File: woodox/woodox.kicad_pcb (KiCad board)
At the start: 2 copper layers, 162.2 x 126.5 mm, 95 parts, among them IC1 W25Q16JVUXIQ_TR, J1 Conn_01x03_Female, J2 USB_C_Receptacle, SW1 BOOT, SW2 RESET, U1 DRV5057A3, U10 OLED_256x64_I2C, U11 DRV5057A3, U12 DRV5057A3, U13 DRV5057A3, U14 DRV5057A3, U15 DRV5057A3, U16 DRV5057A3, U17 DRV5057A3, U18 DRV5057A3, U19 DRV5057A3, U2 DRV5057A3, U20 DRV5057A3, U21 DRV5057A3, U22 DRV5057A3, U23 DRV5057A3, U24 DRV5057A3, U25 RP2040, U26 DRV5057A3, U27 DRV5057A3, U28 DRV5057A3, U29 DRV5057A3, U3 DRV5057A3, U30 DRV5057A3, U31 DRV5057A3, U32 DRV5057A3, U33 NCP1117-3.3_SOT223, U34 74HC4051, U35 74HC4051, U36 74HC4051, U37 74HC4051, U38 DRV5057A3, U39 DRV5057A3, U4 DRV5057A3, U5 DRV5057A3, U6 DRV5057A3, U7 DRV5057A3, U8 DRV5057A3, U9 DRV5057A3, Y1 ECS-120-8-30-JGN-TR

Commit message: double sided pcb
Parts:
- added C11: 0.1uF, Capacitor_SMD:C_0603_1608Metric, F.Cu at (157.4, 56.4)
- added C12: 27pF, Capacitor_SMD:C_0603_1608Metric, F.Cu at (165.9, 74.1)
- added C13: 27pF, Capacitor_SMD:C_0603_1608Metric, F.Cu at (160.3, 71.8)
- added C14: 1uF, Capacitor_SMD:C_0603_1608Metric, F.Cu at (167.5, 59.4)
- added C15: 1uF, Capacitor_SMD:C_0603_1608Metric, F.Cu at (168.6, 62.4)
- added C16: 10uF, Capacitor_SMD:C_0603_1608Metric, F.Cu at (49.4, 33.0)
- added C17: 0.1uF, Capacitor_SMD:C_0603_1608Metric, F.Cu at (167.5, 57.9)
- added C18: 1uF, Capacitor_SMD:C_0603_1608Metric, F.Cu at (167.5, 60.9)
- added C19: 0.1uF, Capacitor_SMD:C_0603_1608Metric, F.Cu at (167.5, 56.4)
- added C20: 10uF, Capacitor_SMD:C_0603_1608Metric, F.Cu at (49.3, 38.4)
- added IC2: W25Q16JVUXIQ_TR, W25Q16JVUXIQ_TR:SON50P300X200X60-9N, F.Cu at (158.9, 57.9)
- added J4: USB_C_Receptacle, Connector_USB:USB_C_Receptacle_Amphenol_12401610E4-2A, F.Cu at (56.2, 35.0)
- added JP1: SolderJumper_2_Open, Jumper:SolderJumper-2_P1.3mm_Open_Pad1.0x1.5mm, B.Cu at (155.0, 92.5)
- added JP2: SolderJumper_2_Open, Jumper:SolderJumper-2_P1.3mm_Open_Pad1.0x1.5mm, B.Cu at (157.5, 92.5)
- added JP3: SolderJumper_2_Open, Jumper:SolderJumper-2_P1.3mm_Open_Pad1.0x1.5mm, F.Cu at (155.0, 92.5)
- added JP4: SolderJumper_2_Open, Jumper:SolderJumper-2_P1.3mm_Open_Pad1.0x1.5mm, F.Cu at (157.5, 92.5)
- added JP5: SolderJumper_2_Open, Jumper:SolderJumper-2_P1.3mm_Open_Pad1.0x1.5mm, F.Cu at (165.3, 92.0)
- added JP6: SolderJumper_2_Open, Jumper:SolderJumper-2_P1.3mm_Open_Pad1.0x1.5mm, B.Cu at (165.3, 92.0)
- added LED33: MX_SK6812MINI-E, lib:LED_MX_SK6812MINI-R, F.Cu at (45.3, 48.6)
- added LED34: MX_SK6812MINI-E, lib:LED_MX_SK6812MINI-R, F.Cu at (45.3, 67.7)
- added LED35: MX_SK6812MINI-E, lib:LED_MX_SK6812MINI-R, F.Cu at (45.3, 86.7)
- added LED36: MX_SK6812MINI-E, lib:LED_MX_SK6812MINI-R, F.Cu at (45.3, 105.8)
- added LED37: MX_SK6812MINI-E, lib:LED_MX_SK6812MINI-R, F.Cu at (57.3, 124.8)
- added LED38: MX_SK6812MINI-E, lib:LED_MX_SK6812MINI-R, F.Cu at (66.9, 48.6)
- added LED39: MX_SK6812MINI-E, lib:LED_MX_SK6812MINI-R, F.Cu at (66.9, 67.7)
- added LED40: MX_SK6812MINI-E, lib:LED_MX_SK6812MINI-R, F.Cu at (66.9, 86.7)
- added LED41: MX_SK6812MINI-E, lib:LED_MX_SK6812MINI-R, F.Cu at (66.9, 105.8)
- added LED42: MX_SK6812MINI-E, lib:LED_MX_SK6812MINI-R, F.Cu at (85.9, 44.2)
- added LED43: MX_SK6812MINI-E, lib:LED_MX_SK6812MINI-R, F.Cu at (85.9, 63.2)
- added LED44: MX_SK6812MINI-E, lib:LED_MX_SK6812MINI-R, F.Cu at (85.9, 82.3)
- added LED45: MX_SK6812MINI-E, lib:LED_MX_SK6812MINI-R, F.Cu at (85.9, 101.3)
- added LED46: MX_SK6812MINI-E, lib:LED_MX_SK6812MINI-R, F.Cu at (85.9, 120.4)
- added LED47: MX_SK6812MINI-E, lib:LED_MX_SK6812MINI-R, F.Cu at (105.0, 41.6)
- added LED48: MX_SK6812MINI-E, lib:LED_MX_SK6812MINI-R, F.Cu at (105.0, 60.7)
- added LED49: MX_SK6812MINI-E, lib:LED_MX_SK6812MINI-R, F.Cu at (105.0, 79.7)
- added LED50: MX_SK6812MINI-E, lib:LED_MX_SK6812MINI-R, F.Cu at (105.0, 98.8)
- added LED51: MX_SK6812MINI-E, lib:LED_MX_SK6812MINI-R, F.Cu at (105.0, 117.8)
- added LED52: MX_SK6812MINI-E, lib:LED_MX_SK6812MINI-R, F.Cu at (124.0, 44.2)
- added LED53: MX_SK6812MINI-E, lib:LED_MX_SK6812MINI-R, F.Cu at (124.0, 63.2)
- added LED54: MX_SK6812MINI-E, lib:LED_MX_SK6812MINI-R, F.Cu at (124.0, 82.3)
- added LED55: MX_SK6812MINI-E, lib:LED_MX_SK6812MINI-R, F.Cu at (124.0, 101.3)
- added LED56: MX_SK6812MINI-E, lib:LED_MX_SK6812MINI-R, F.Cu at (130.2, 123.6)
- added LED57: MX_SK6812MINI-E, lib:LED_MX_SK6812MINI-R, F.Cu at (143.1, 46.1)
- added LED58: MX_SK6812MINI-E, lib:LED_MX_SK6812MINI-R, F.Cu at (143.1, 65.1)
- added LED59: MX_SK6812MINI-E, lib:LED_MX_SK6812MINI-R, F.Cu at (143.1, 84.2)
- added LED60: MX_SK6812MINI-E, lib:LED_MX_SK6812MINI-R, F.Cu at (143.1, 103.2)
- added LED61: MX_SK6812MINI-E, lib:LED_MX_SK6812MINI-R, F.Cu at (165.6, 109.6)
- added LED62: MX_SK6812MINI-E, lib:LED_MX_SK6812MINI-R, F.Cu at (153.5, 130.5)
- added LED63: MX_SK6812MINI-E, lib:LED_MX_SK6812MINI-R, F.Cu at (182.1, 119.1)
- added LED64: MX_SK6812MINI-E, lib:LED_MX_SK6812MINI-R, F.Cu at (170.0, 140.0)
- added R10: 10k, Resistor_SMD:R_0603_1608Metric, F.Cu at (157.3, 62.0)
- added R11: 1k, Resistor_SMD:R_0603_1608Metric, F.Cu at (165.1, 71.8)
- added R12: 27.4, Resistor_SMD:R_0603_1608Metric, F.Cu at (164.9, 57.2)
- added R13: 27.4, Resistor_SMD:R_0603_1608Metric, F.Cu at (163.4, 57.2)
- added R14: 5k1, Resistor_SMD:R_0603_1608Metric, F.Cu at (63.1, 35.3)
- added R15: 5k1, Resistor_SMD:R_0603_1608Metric, F.Cu at (64.7, 35.3)
- added R16: 1k, Resistor_SMD:R_0603_1608Metric, F.Cu at (170.1, 46.1)
- added R9: 1k, Resistor_SMD:R_0603_1608Metric, F.Cu at (170.1, 50.0)
- added SW3: BOOT, Button_Switch_SMD:SW_Push_1P1T_NO_Vertical_Wuerth_434133025816, F.Cu at (166.5, 50.0)
- added SW4: RESET, Button_Switch_SMD:SW_Push_1P1T_NO_Vertical_Wuerth_434133025816, F.Cu at (166.5, 46.1)
- added U40: DRV5057A3, lib:DRV505x, F.Cu at (45.3, 48.6)
- added U41: DRV5057A3, lib:DRV505x, F.Cu at (45.3, 67.6)
- added U42: DRV5057A3, lib:DRV505x, F.Cu at (45.3, 86.7)
- added U43: DRV5057A3, lib:DRV505x, F.Cu at (45.3, 105.7)
- added U44: DRV5057A3, lib:DRV505x, F.Cu at (57.4, 124.8)
- added U45: DRV5057A3, lib:DRV505x, F.Cu at (66.9, 48.6)
- added U46: DRV5057A3, lib:DRV505x, F.Cu at (66.9, 67.6)
- added U47: DRV5057A3, lib:DRV505x, F.Cu at (66.9, 86.7)
- added U48: DRV5057A3, lib:DRV505x, F.Cu at (66.9, 105.7)
- added U50: DRV5057A3, lib:DRV505x, F.Cu at (86.0, 44.2)
- added U51: DRV5057A3, lib:DRV505x, F.Cu at (86.0, 63.2)
- added U52: DRV5057A3, lib:DRV505x, F.Cu at (86.0, 82.3)
- added U53: DRV5057A3, lib:DRV505x, F.Cu at (86.0, 101.3)
- added U54: DRV5057A3, lib:DRV505x, F.Cu at (86.0, 120.3)
- added U55: DRV5057A3, lib:DRV505x, F.Cu at (105.0, 41.6)
- added U56: DRV5057A3, lib:DRV505x, F.Cu at (105.0, 60.7)
- added U57: DRV5057A3, lib:DRV505x, F.Cu at (105.0, 79.7)
- added U58: DRV5057A3, lib:DRV505x, F.Cu at (105.0, 98.8)
- added U59: DRV5057A3, lib:DRV505x, F.Cu at (105.0, 117.8)
- added U60: DRV5057A3, lib:DRV505x, F.Cu at (124.1, 44.2)
- added U61: DRV5057A3, lib:DRV505x, F.Cu at (124.1, 63.2)
- added U62: DRV5057A3, lib:DRV505x, F.Cu at (124.1, 82.3)
- added U63: DRV5057A3, lib:DRV505x, F.Cu at (124.1, 101.3)
- added U64: RP2040, Package_DFN_QFN:QFN-56-1EP_7x7mm_P0.4mm_EP3.2x3.2mm, F.Cu at (162.9, 65.5)
- added U65: DRV5057A3, lib:DRV505x, F.Cu at (130.2, 123.5)
- added U66: DRV5057A3, lib:DRV505x, F.Cu at (143.1, 46.1)
- added U67: DRV5057A3, lib:DRV505x, F.Cu at (143.1, 65.1)
- added U68: DRV5057A3, lib:DRV505x, F.Cu at (143.1, 84.2)
- added U69: DRV5057A3, lib:DRV505x, F.Cu at (143.1, 103.2)
- added U70: DRV5057A3, lib:DRV505x, F.Cu at (165.7, 109.6)
- added U71: DRV5057A3, lib:DRV505x, F.Cu at (153.6, 130.5)
- added U72: NCP1117-3.3_SOT223, Package_TO_SOT_SMD:SOT-223-3_TabPin2, F.Cu at (43.2, 35.5)
- added U73: 74HC4051, Package_SO:TSSOP-16_4.4x5mm_P0.65mm, F.Cu at (149.9, 53.3)
- added U74: 74HC4051, Package_SO:TSSOP-16_4.4x5mm_P0.65mm, F.Cu at (149.9, 72.5)
- added U75: 74HC4051, Package_SO:TSSOP-16_4.4x5mm_P0.65mm, F.Cu at (149.9, 91.5)
- added U76: 74HC4051, Package_SO:TSSOP-16_4.4x5mm_P0.65mm, F.Cu at (149.9, 110.8)
- added U77: DRV5057A3, lib:DRV505x, F.Cu at (182.1, 119.2)
- added U78: DRV5057A3, lib:DRV505x, F.Cu at (170.1, 140.0)
- added Y2: ECS-120-8-30-JGN-TR, Crystal:Crystal_SMD_5032-2Pin_5.0x3.2mm, F.Cu at (161.9, 74.7)
- moved J1 7.49 mm to (169.0, 91.5), turned to 0 degrees
- moved R8 5.98 mm to (170.1, 46.1), turned to -90 degrees
- moved R1 5.15 mm to (170.1, 50.0), turned to -90 degrees
- moved SW2 3.42 mm to (166.4, 46.1), turned to 0 degrees
- moved SW1 2.07 mm to (166.5, 50.0), turned to 0 degrees
- moved R4 1.04 mm to (160.7, 57.8)
- moved R5 1.04 mm to (162.3, 57.7)
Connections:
- net /D_SCL renamed /D_RST_R
- net Net-(J1-Pin_2) renamed /SWD
- net Net-(J1-Pin_3) renamed /SWCLK
- net Net-(J2-D+-PadA6) renamed /USB_D+
- net Net-(J2-D--PadA7) renamed /USB_D-
- J1 pad 1: +3.3V -> Net-(J1-Pin_1)
- U10 pad 1: GND -> /D_CS_R
- U10 pad 2: +3.3V -> /D_DC_R
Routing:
- net +3.3VR: track 0.00 -> 1090.9 mm, vias 0 -> 46
- net +5V: track 789.0 -> 1508.9 mm, vias 40 -> 81
- net Net-(U44-OUT): track 0.00 -> 215.0 mm
- net Net-(U54-OUT): track 0.00 -> 144.9 mm, vias 0 -> 2
- net Net-(U42-OUT): track 0.00 -> 116.2 mm
- net Net-(U43-OUT): track 0.00 -> 115.4 mm
- net Net-(U41-OUT): track 0.00 -> 114.4 mm
- net Net-(U40-OUT): track 0.00 -> 111.7 mm
- net /MUX R E: track 0.00 -> 110.8 mm, vias 0 -> 5
- net Net-(U59-OUT): track 0.00 -> 110.3 mm, vias 0 -> 2
- net /MUX R S0: track 0.00 -> 104.4 mm, vias 0 -> 5
- net /MUX R S2: track 0.00 -> 104.0 mm, vias 0 -> 5
- net /MUX R S1: track 0.00 -> 103.8 mm, vias 0 -> 5
- net +3.3V: track 952.1 -> 1053.4 mm
- net Net-(U47-OUT): track 0.00 -> 93.8 mm
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- added copper zone on In1.Cu, net GND
- added copper zone on In2.Cu, net GND
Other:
- copper layers 2 -> 4

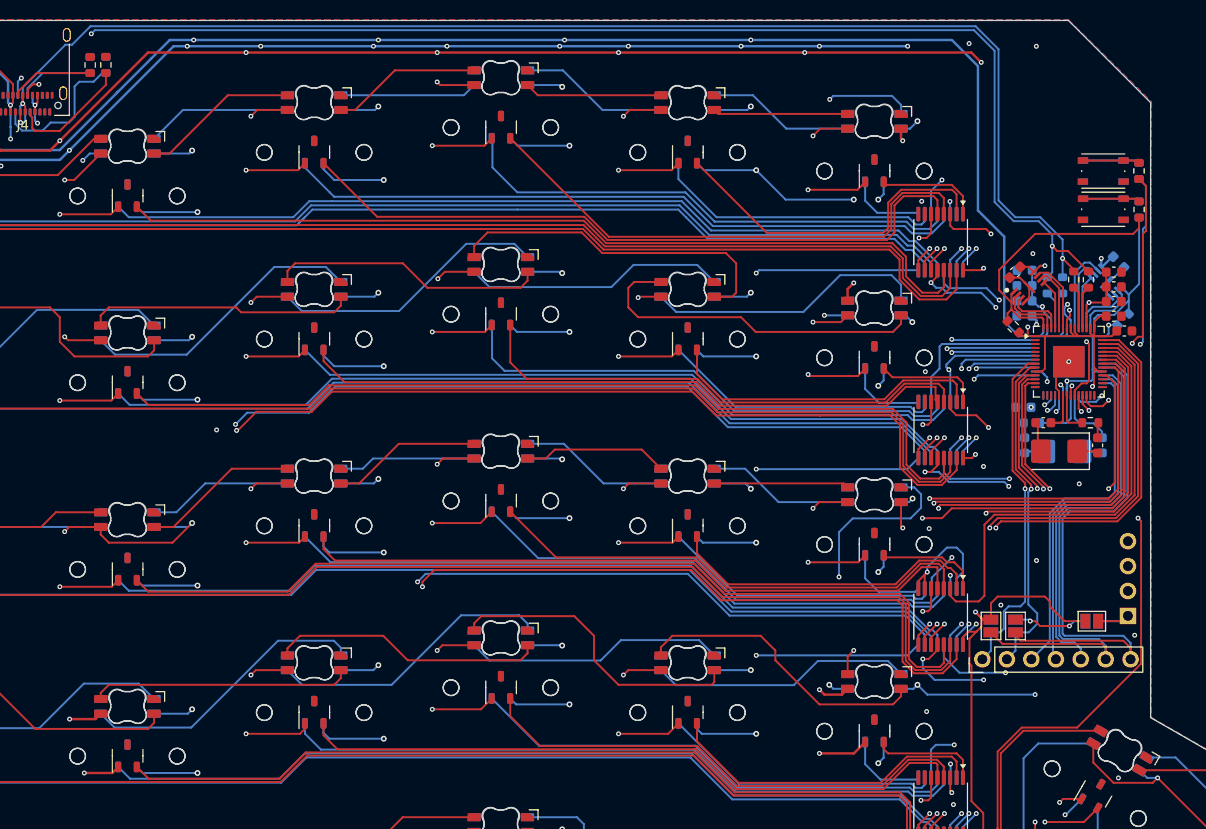
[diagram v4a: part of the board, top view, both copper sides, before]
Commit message: usb-c interconnects and expansion solder pads
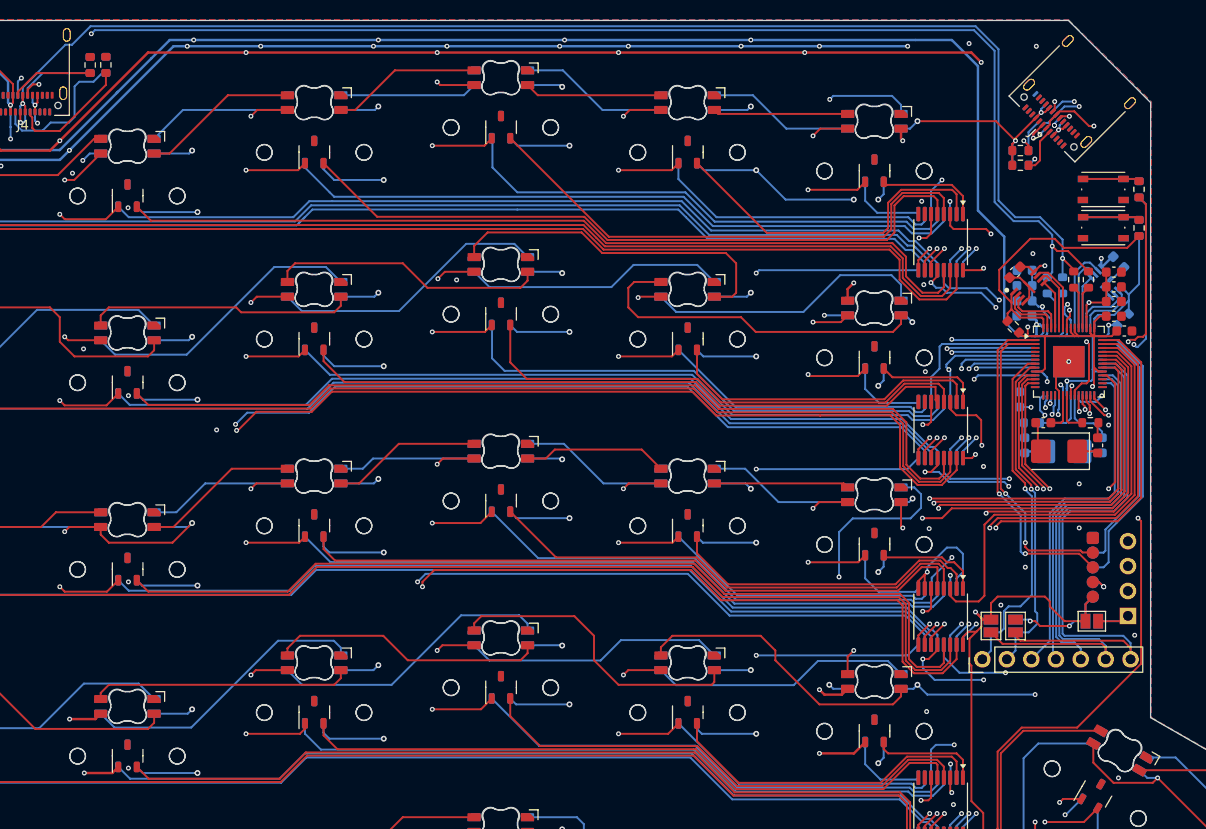
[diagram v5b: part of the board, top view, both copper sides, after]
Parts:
- added J5: Conn_01x05_Socket, lib:TestPad_5pins, F.Cu at (165.4, 86.5)
- added J6: USB_C_Interlink, Connector_USB:USB_C_Receptacle_Amphenol_12401610E4-2A, B.Cu at (164.0, 38.0)
- added J7: USB_C_Interlink, Connector_USB:USB_C_Receptacle_Amphenol_12401610E4-2A, F.Cu at (164.0, 38.0)
- added J8: Conn_01x05_Socket, lib:TestPad_5pins, B.Cu at (165.4, 86.5)
- added R17: 56k, Resistor_SMD:R_0603_1608Metric, B.Cu at (158.0, 44.0)
- added R18: 56k, Resistor_SMD:R_0603_1608Metric, B.Cu at (158.0, 45.5)
- added R19: 56k, Resistor_SMD:R_0603_1608Metric, F.Cu at (158.0, 44.0)
- added R20: 56k, Resistor_SMD:R_0603_1608Metric, F.Cu at (158.0, 45.5)
- J2, J4: value USB_C_Receptacle -> USB_C_To_Host
- moved R1 1.88 mm to (170.1, 51.9)
- moved R16 1.88 mm to (170.1, 48.0)
- moved R8 1.88 mm to (170.1, 48.0)
- moved R9 1.88 mm to (170.1, 51.9)
- moved SW1 1.88 mm to (166.5, 51.9)
- moved SW2 1.88 mm to (166.4, 48.0)
- moved SW3 1.88 mm to (166.5, 51.9)
- moved SW4 1.88 mm to (166.5, 48.0)
- moved C5 0.89 mm to (157.9, 69.4), turned to 90 degrees
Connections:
- U25 pad 2: unconnected-(U25-GPIO0-Pad2) -> /I2C ACC SDA
- U25 pad 27: unconnected-(U25-GPIO16-Pad27) -> /I2C SDA
- U25 pad 28: unconnected-(U25-GPIO17-Pad28) -> /I2C SDL
- U25 pad 3: unconnected-(U25-GPIO1-Pad3) -> /I2C ACC SDL
- U64 pad 2: unconnected-(U64-GPIO0-Pad2) -> /I2C ACC R SDA
- U64 pad 27: unconnected-(U64-GPIO16-Pad27) -> /I2C R SDA
- U64 pad 28: unconnected-(U64-GPIO17-Pad28) -> /I2C R SDL
- U64 pad 3: unconnected-(U64-GPIO1-Pad3) -> /I2C ACC R SDL
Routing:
- net /I2C SDA: track 0.00 -> 59.1 mm, vias 0 -> 3
- net /I2C SDL: track 0.00 -> 53.6 mm, vias 0 -> 3
- net /I2C R SDA: track 0.00 -> 50.8 mm, vias 0 -> 3
- net +5V: track 1508.9 -> 1556.3 mm, vias 81 -> 86
- net /I2C R SDL: track 0.00 -> 44.7 mm, vias 0 -> 2
- net /I2C ACC R SDA: track 0.00 -> 33.8 mm, vias 0 -> 2
- net /I2C ACC R SDL: track 0.00 -> 31.9 mm, vias 0 -> 2
- net /I2C ACC SDA: track 0.00 -> 28.5 mm
- net /I2C ACC SDL: track 0.00 -> 26.3 mm
- net Net-(J7-CC2): track 0.00 -> 7.58 mm, vias 0 -> 2
- net Net-(J6-CC2): track 0.00 -> 6.12 mm, vias 0 -> 3
- net +3.3V: track 1053.4 -> 1059.5 mm
- net Net-(J7-CC1): track 0.00 -> 4.71 mm
- net +3.3VR: track 1090.9 -> 1095.0 mm
- net Net-(J6-CC1): track 0.00 -> 3.43 mm
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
